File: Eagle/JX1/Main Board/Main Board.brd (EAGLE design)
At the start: 50.8 x 76.2 mm, 9 parts, among them J1 RASPBERRYPI-40-PIN-GPIO_PTH_N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, U1 SN74HC595N, U2 SN74HC595N

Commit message: More board Changes
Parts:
- removed J1: RASPBERRYPI-40-PIN-GPIO_PTH_NO_SHROUD, SparkFun-Connectors:2X20
- added POWER_CONN, SERIAL_CONN: (no value), pinhead:1X03
- moved B4 86.7 mm to (83.8, 64.8), turned to 90 degrees
- moved POWER 71.0 mm to (77.5, 12.7), turned to 270 degrees
- moved B3 52.4 mm to (62.2, 64.8), turned to 90 degrees
- moved MODUL1 47.4 mm to (29.2, 11.4), turned to 270 degrees
- moved U2 41.4 mm to (52.1, 39.4)
- moved U1 33.6 mm to (25.4, 39.4), turned to 180 degrees
- moved B2 22.8 mm to (40.6, 64.8), turned to 90 degrees
- moved B1 12.6 mm to (19.1, 64.8), turned to 90 degrees
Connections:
- net N$19 renamed SCK
- net N$20 renamed MOSI
- net N$21 renamed MISO
- net N$23 renamed SSCK
- net N$24 renamed SCL
- net N$25 renamed RCK
- removed net 3.3V: J1.1, J1.17
- removed net N$26: J1.10, MODUL1.J1.1
- new net N$1: MODUL1.J1.1, SERIAL_CONN.2
- net +5V: now also POWER_CONN.2; no longer J1.2, J1.4
- net GND: now also POWER_CONN.1, POWER_CONN.3; no longer J1.14, J1.20, J1.25, J1.30, J1.34, J1.39, J1.6, J1.9
- net N$27: now also SERIAL_CONN.1, SERIAL_CONN.3; no longer J1.8
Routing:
- net SCK: track 0.00 -> 129.2 mm
- net MISO: track 0.00 -> 124.5 mm
- net MOSI: track 0.00 -> 113.0 mm
- net +5V: track 0.00 -> 101.5 mm
- net RCK: track 0.00 -> 99.4 mm
- net N$2: track 0.00 -> 90.7 mm
- net SSCK: track 0.00 -> 64.1 mm
- net SCL: track 0.00 -> 53.6 mm
- net +12V: track 0.00 -> 42.9 mm
- net N$27: track 0.00 -> 25.1 mm
- net N$22: track 0.00 -> 19.7 mm
- net N$1: track 0.00 -> 12.9 mm
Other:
- board size 50.8 x 76.2 mm -> 101.6 x 76.2 mm

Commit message: Schematic and board changes
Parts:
- turned SERIAL_CONN to 90 degrees
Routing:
- net SCK: track 129.2 -> 0.00 mm
- net MISO: track 124.5 -> 0.00 mm
- net MOSI: track 113.0 -> 0.00 mm
- net +5V: track 101.5 -> 0.00 mm
- net RCK: track 99.4 -> 0.00 mm
- net N$2: track 90.7 -> 0.00 mm
- net SSCK: track 64.1 -> 0.00 mm
- net SCL: track 53.6 -> 0.00 mm
- net +12V: track 42.9 -> 0.00 mm
- net N$27: track 25.1 -> 0.00 mm
- net N$22: track 19.7 -> 0.00 mm
- net N$1: track 12.9 -> 13.5 mm

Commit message: Hand-routing the board
Made changes to pin connections for better, neater routing.
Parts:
- moved U2 19.1 mm to (71.1, 40.6)
- moved MODUL1 3.81 mm to (25.4, 11.4)
- moved U1 2.84 mm to (27.9, 40.6)
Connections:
- removed net N$10: B1.EN, U1.15
- removed net N$12: B4.STEP, U2.6
- removed net N$14: B4.EN, U2.4
- removed net N$17: B3.DIR, U2.1
- removed net N$4: B2.STEP, U1.6
- removed net N$5: B2.DIR, U1.5
- removed net N$6: B2.EN, U1.4
- removed net N$7: B1.CFG3, U1.3
- removed net N$8: B1.STEP, U1.2
- removed net N$9: B1.DIR, U1.1
- new net N$20: B1.DIR, U1.4
- new net N$21: B1.STEP, U1.5
- new net N$23: B1.CFG3, U1.6
- new net N$24: B2.STEP, U1.1
- new net N$25: B2.DIR, U1.15
- new net N$26: B2.EN, U1.3
- new net N$28: B1.EN, U1.7
- new net N$30: B3.DIR, U2.4
- new net N$33: B4.EN, U2.3
- new net N$35: B4.STEP, U2.1
- net N$11: now also B3.EN; no longer B4.CFG3
- net N$13: now also B3.STEP; no longer B4.DIR
- net N$15: now also U2.6; no longer U2.3
- net N$16: now also B4.CFG3; no longer B3.STEP
- net N$18: now also B4.DIR; no longer B3.EN
- net N$3: now also U1.2; no longer U1.7
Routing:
- net +5V: track 0.00 -> 65.3 mm
- net +12V: track 0.00 -> 47.4 mm
- net N$27: track 0.00 -> 28.9 mm
- net N$1: track 13.5 -> 17.3 mm

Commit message: Routed Main Board
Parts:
- moved B1 14.2 mm to (12.7, 52.1)
- moved B2 14.2 mm to (34.3, 52.1)
- moved B3 14.2 mm to (55.9, 52.1)
- moved B4 14.2 mm to (77.5, 52.1)
- moved POWER 12.7 mm to (64.8, 12.7)
- moved POWER_CONN 12.7 mm to (76.2, 12.7)
- moved U2 11.7 mm to (63.5, 31.8)
- moved U1 11.7 mm to (20.3, 31.8)
- moved SERIAL_CONN 5.08 mm to (52.1, 12.7)
- moved MODUL1 1.27 mm to (24.1, 11.4)
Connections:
- new net NC: MODUL1.J2.4
- net +5V: no longer MODUL1.J2.4
- net N$22: now also MODUL1.J1.8; no longer MODUL1.J1.5
- net RCK: now also MODUL1.J1.10; no longer MODUL1.J1.8
- net SCL: now also MODUL1.J1.12; no longer MODUL1.J1.7
- net SSCK: now also MODUL1.J1.11; no longer MODUL1.J1.6
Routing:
- net GND: track 0.00 -> 630.0 mm, vias 0 -> 5
- net +5V: track 65.3 -> 365.1 mm
- net MISO: track 0.00 -> 182.1 mm
- net SCK: track 0.00 -> 166.9 mm
- net +12V: track 47.4 -> 193.4 mm
- net MOSI: track 0.00 -> 140.8 mm
- net SCL: track 0.00 -> 82.1 mm
- net N$2: track 0.00 -> 81.6 mm
- net RCK: track 0.00 -> 77.1 mm
- net SSCK: track 0.00 -> 73.6 mm
- net N$25: track 0.00 -> 26.1 mm
- net N$18: track 0.00 -> 24.6 mm
- net N$24: track 0.00 -> 16.4 mm
- net N$35: track 0.00 -> 15.6 mm
- net N$11: track 0.00 -> 14.7 mm
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- added copper zone on layer 1, net GND
- added copper zone on layer 16, net GND
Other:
- board size 101.6 x 76.2 mm -> 95.2 x 67.3 mm

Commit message: Started moving traces to make room for thermal stuff
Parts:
- added X1, X2: (no value), con-wago-500:W237-102
- moved POWER 13.3 mm to (77.5, 8.89)
- moved POWER_CONN 13.3 mm to (88.9, 8.89)
- moved SERIAL_CONN 4.02 mm to (50.8, 16.5)
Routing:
- net GND: track 630.0 -> 642.3 mm, vias 5 -> 6
- net +5V: track 365.1 -> 358.3 mm
- net +12V: track 193.4 -> 200.3 mm
- net RCK: track 77.1 -> 70.3 mm
- net SSCK: track 73.6 -> 69.3 mm
- net N$1: track 13.5 -> 10.7 mm
- net N$27: track 25.8 -> 23.0 mm
- net SCL: track 82.1 -> 79.5 mm
- net MOSI: track 140.8 -> 140.0 mm

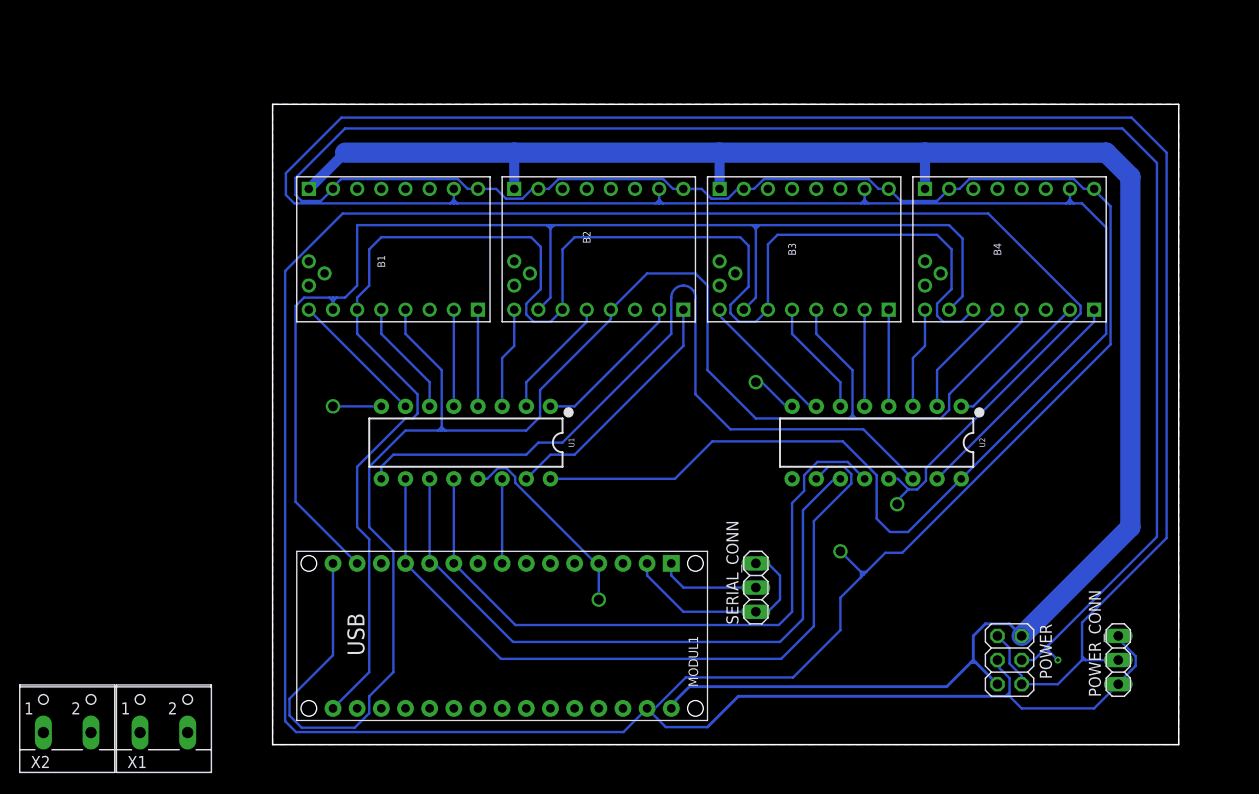
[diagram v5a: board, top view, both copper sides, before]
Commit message: Added and connected thermistor terminals
Also added terminals for bed and extruder, but did not connect them.
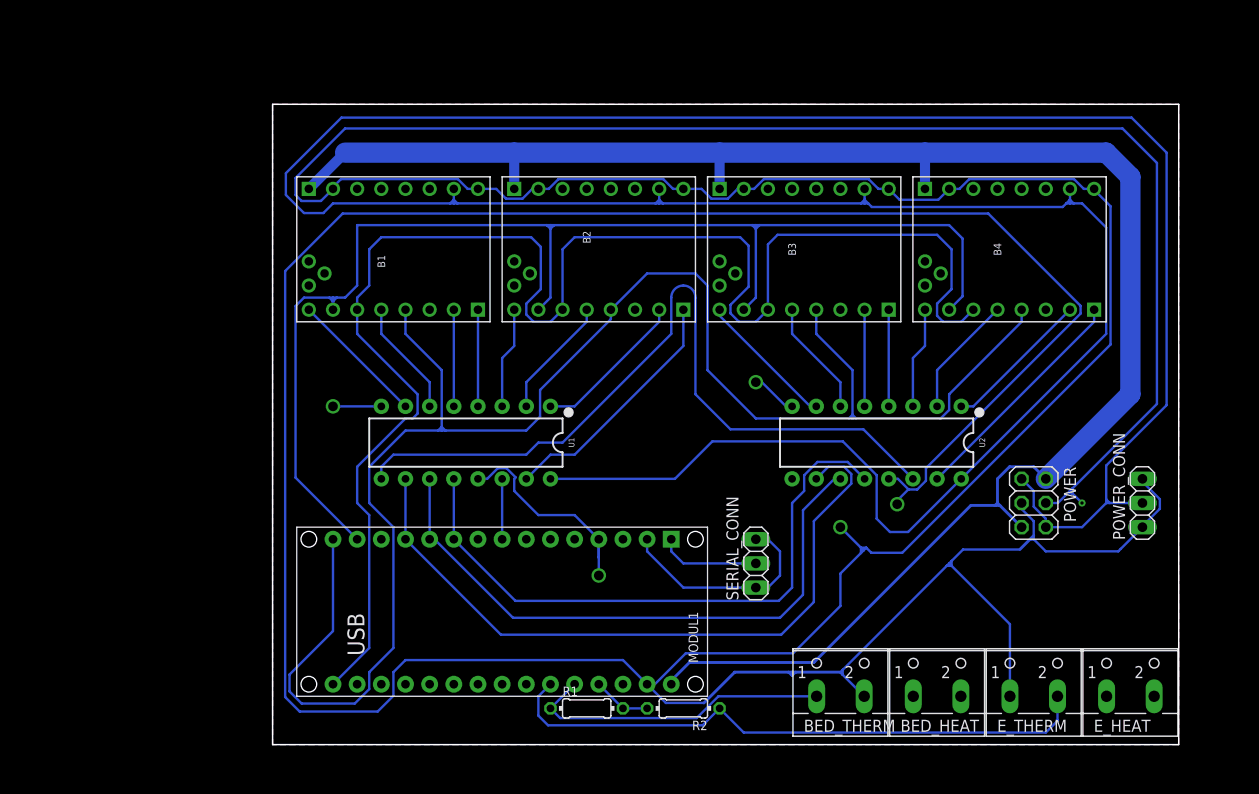
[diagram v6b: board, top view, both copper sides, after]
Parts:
- removed X1, X2: (no value), con-wago-500:W237-102
- added BED_HEAT, BED_THERM, E_HEAT, E_THERM: (no value), con-wago-500:W237-102
- added R1, R2: (no value), eagle-ltspice:0204/7
- moved POWER 16.7 mm to (80.0, 25.4)
- moved POWER_CONN 16.7 mm to (91.4, 25.4)
- moved MODUL1 2.54 mm to (24.1, 14.0)
- moved SERIAL_CONN 2.54 mm to (50.8, 19.1)
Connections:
- removed net NC: MODUL1.J2.4
- new net ARD_5V: MODUL1.J2.4, R1.2, R2.2
- new net BED_THERM_CON: BED_THERM.1, MODUL1.J2.5, R1.1
- new net E_THERM_CON: E_THERM.2, MODUL1.J2.6, R2.1
- net GND: now also BED_THERM.2, E_THERM.1
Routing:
- net E_THERM_CON: track 0.00 -> 63.7 mm
- net BED_THERM_CON: track 0.00 -> 32.9 mm
- net +5V: track 358.3 -> 341.9 mm
- net GND: track 642.3 -> 658.5 mm
- net +12V: track 200.3 -> 191.0 mm
- net ARD_5V: track 0.00 -> 6.13 mm
- net SSCK: track 69.3 -> 64.2 mm
- net SCL: track 79.5 -> 74.5 mm
- net RCK: track 70.3 -> 65.2 mm
- net SCK: track 166.9 -> 164.4 mm
- net MISO: track 182.1 -> 179.5 mm
- net N$22: track 8.89 -> 6.35 mm
- net MOSI: track 140.0 -> 137.4 mm

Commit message: Beefed up 12V in traces
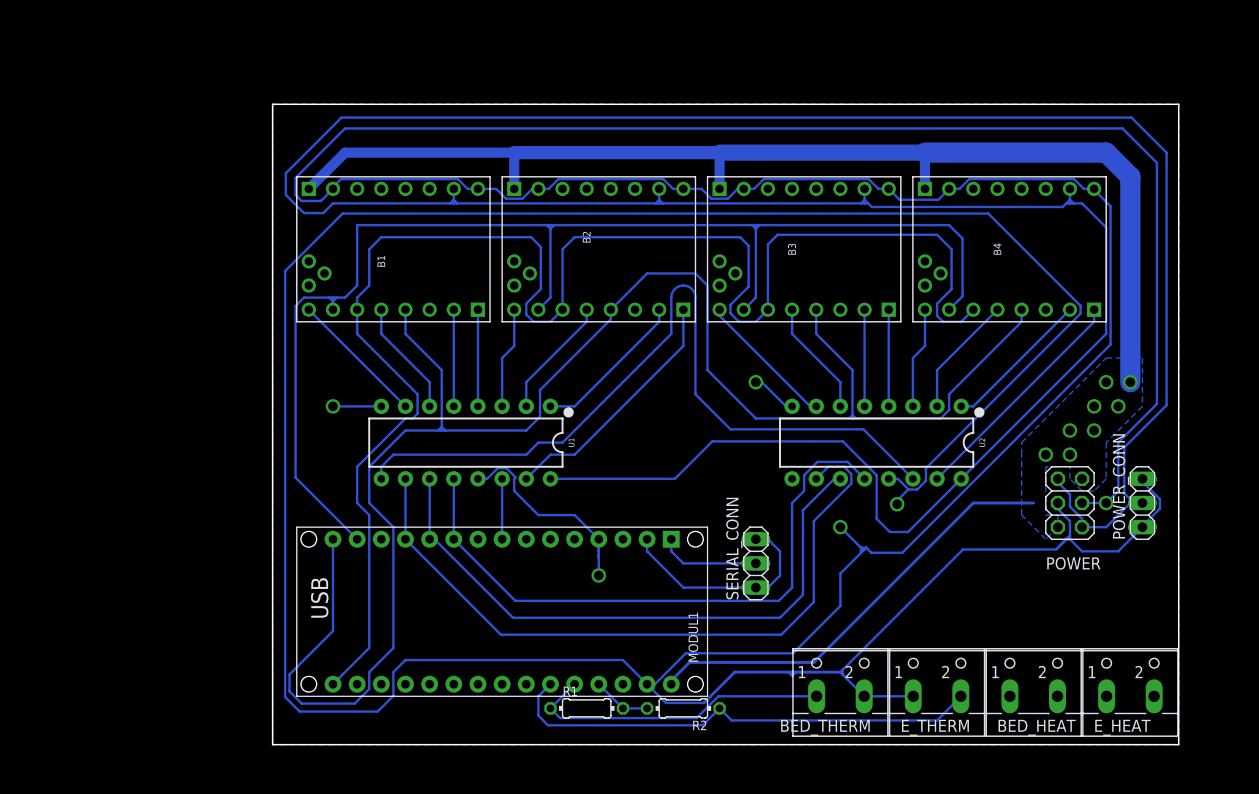
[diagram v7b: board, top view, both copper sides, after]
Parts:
- moved BED_HEAT 10.2 mm to (80.0, 6.35)
- moved E_THERM 10.2 mm to (69.8, 6.35)
- moved POWER 3.81 mm to (83.8, 25.4)
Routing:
- net +12V: track 191.0 -> 168.2 mm, vias 0 -> 8
- net GND: track 658.5 -> 642.3 mm
- net E_THERM_CON: track 63.7 -> 51.0 mm
- net +5V: track 341.9 -> 337.5 mm
- added copper zone on layer 16, net +12V

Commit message: Worked on heater traces some more.
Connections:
- net +12V: now also BED_HEAT.2, E_HEAT.1
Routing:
- net +12V: vias 8 -> 12
- added copper zone on layer 1, net +12V
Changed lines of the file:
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@@
 <wire x1="53.975" y1="35.56" x2="51.435" y2="38.1" width="0.254" layer="16"/>
 <wire x1="51.435" y1="38.1" x2="50.8" y2="38.1" width="0.254" layer="16"/>
-<polygon width="0.254" layer="1" isolate="1.016">
+<polygon width="0.254" layer="1" isolate="1.016" rank="2">
 <vertex x="0" y="67.31"/>
 <vertex x="95.25" y="67.31"/>
@@
 <wire x1="54.991" y1="7.62" x2="59.69" y2="7.62" width="0.3048" layer="16"/>
 <wire x1="83.439" y1="21.59" x2="83.82" y2="21.59" width="0.3048" layer="16"/>
-<wire x1="82.3595" y1="20.5105" x2="83.439" y2="21.59" width="0.3048" layer="16"/>
 <wire x1="83.439" y1="21.59" x2="83.82" y2="21.971" width="0.3048" layer="16"/>
 <wire x1="11.049" y1="3.4798" x2="12.7" y2="5.1308" width="0.254" layer="16"/>
@@
 <wire x1="54.61" y1="7.239" x2="54.991" y2="7.62" width="0.254" layer="16"/>
 <wire x1="59.69" y1="7.62" x2="59.924" y2="7.854" width="0.254" layer="16"/>
-<wire x1="59.924" y1="7.854" x2="72.5805" y2="20.5105" width="0.254" layer="16"/>
-<wire x1="72.5805" y1="20.5105" x2="82.3595" y2="20.5105" width="0.254" layer="16"/>
+<wire x1="59.924" y1="7.854" x2="73.66" y2="21.59" width="0.254" layer="16"/>
+<wire x1="73.66" y1="21.59" x2="83.439" y2="21.59" width="0.254" layer="16"/>
 <contactref element="E_THERM" pad="1"/>
 <contactref element="BED_THERM" pad="2"/>
@@
 <vertex x="83.82" y="27.94"/>
 <vertex x="83.82" y="29.21"/>
-<vertex x="82.55" y="29.21"/>
 <vertex x="81.28" y="29.21"/>
 <vertex x="81.28" y="24.13"/>
 <vertex x="82.55" y="24.13"/>
 <vertex x="82.55" y="22.86"/>
-<vertex x="81.28" y="21.59"/>
-<vertex x="78.74" y="24.13"/>
-<vertex x="78.74" y="30.48"/>
+<vertex x="81.915" y="22.225"/>
+<vertex x="78.74" y="22.225"/>
 <vertex x="78.74" y="31.75"/>
 </polygon>
 <wire x1="73.66" y1="25.4" x2="80.01" y2="25.4" width="0.3048" layer="16"/>
 <wire x1="56.896" y1="8.636" x2="73.66" y2="25.4" width="0.3048" layer="16"/>
-<via x="81.28" y="30.48" extent="1-16" drill="1.02"/>
+<via x="80.01" y="24.13" extent="1-16" drill="1.02"/>
 <via x="83.82" y="30.48" extent="1-16" drill="1.02" diameter="1.02"/>
+<polygon width="0.1524" layer="1">
+<vertex x="87.63" y="40.64"/>
+<vertex x="90.17" y="40.64"/>
+<vertex x="91.44" y="39.37"/>
+<vertex x="91.44" y="35.56"/>
+<vertex x="87.63" y="31.75"/>
+<vertex x="87.63" y="27.94"/>
+<vertex x="86.36" y="26.67"/>
+<vertex x="85.09" y="26.67"/>
+<vertex x="83.82" y="27.94"/>
+<vertex x="83.82" y="29.21"/>
+<vertex x="81.28" y="29.21"/>
+<vertex x="81.28" y="24.13"/>
+<vertex x="82.55" y="24.13"/>
+<vertex x="83.82" y="22.86"/>
+<vertex x="83.82" y="19.05"/>
+<vertex x="90.17" y="12.7"/>
+<vertex x="90.17" y="2.54"/>
+<vertex x="80.01" y="2.54"/>
+<vertex x="80.01" y="8.89"/>
+<vertex x="74.93" y="13.97"/>
+<vertex x="74.93" y="27.94"/>
+</polygon>
+<contactref element="E_HEAT" pad="1"/>
+<contactref element="BED_HEAT" pad="2"/>
+<via x="80.01" y="11.43" extent="1-16" drill="1.02"/>
+<via x="82.55" y="11.43" extent="1-16" drill="1.02"/>
+<via x="86.36" y="11.43" extent="1-16" drill="1.02"/>
+<via x="88.9" y="11.43" extent="1-16" drill="1.02"/>
+<polygon width="0.1524" layer="16">
+<vertex x="80.01" y="2.54"/>
+<vertex x="80.01" y="8.89"/>
+<vertex x="78.74" y="10.16"/>
+<vertex x="78.74" y="12.7"/>
+<vertex x="90.17" y="12.7"/>
+<vertex x="90.17" y="2.54"/>
+</polygon>
 </signal>
 <signal name="SCK">
